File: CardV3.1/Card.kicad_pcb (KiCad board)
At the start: 2 copper layers, 85.6 x 54 mm, 6 parts, among them U1 M24LR04E-R

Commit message: Update Card.kicad_pcb
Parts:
- moved D1 2.01 mm to (119.0, 70.8)
- moved R1 1.25 mm to (114.0, 70.7)
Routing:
- net Net-(D1-Pad2): track 4.23 -> 3.44 mm
- net +3V3: track 7.20 -> 7.72 mm
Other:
- board text added: "Designed by Tingliang, Copyright © 2021 Tingliang Zhang CC BY-NC-ND"

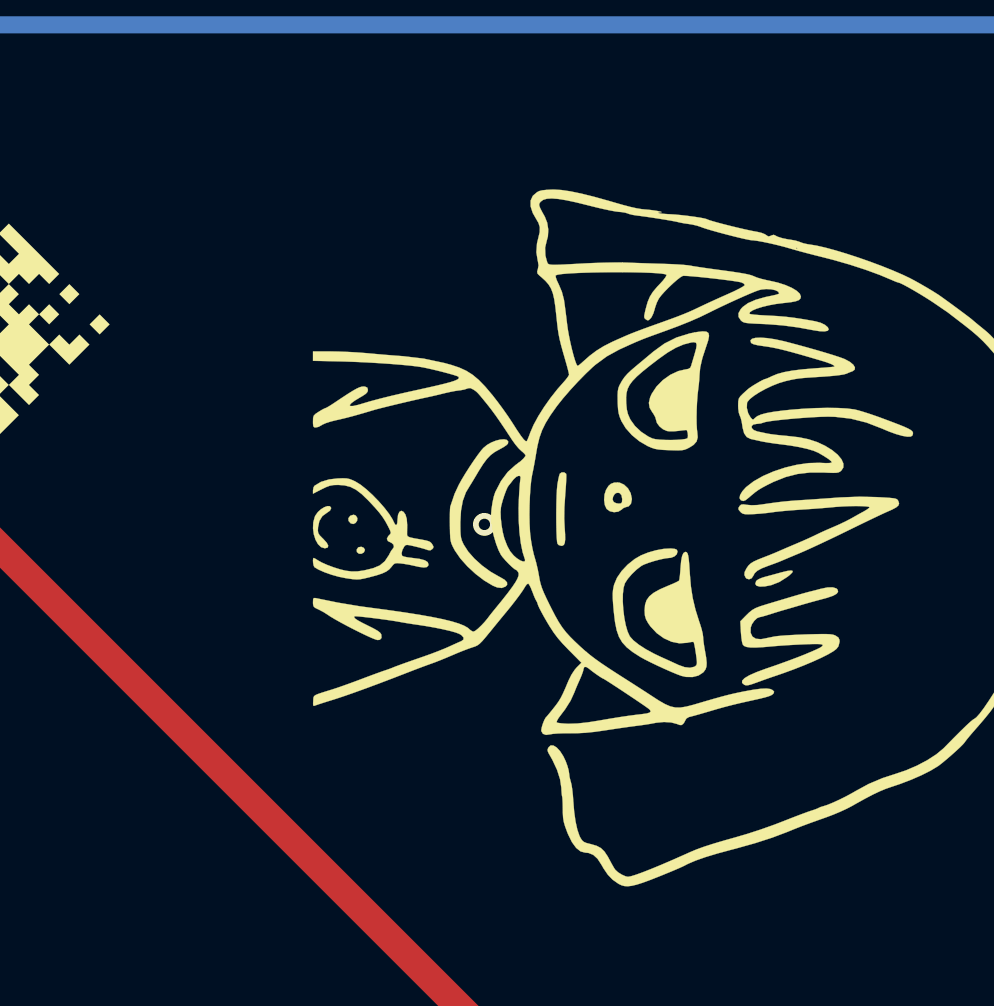
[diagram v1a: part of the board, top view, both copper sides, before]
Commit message: Add Interaction LOGO
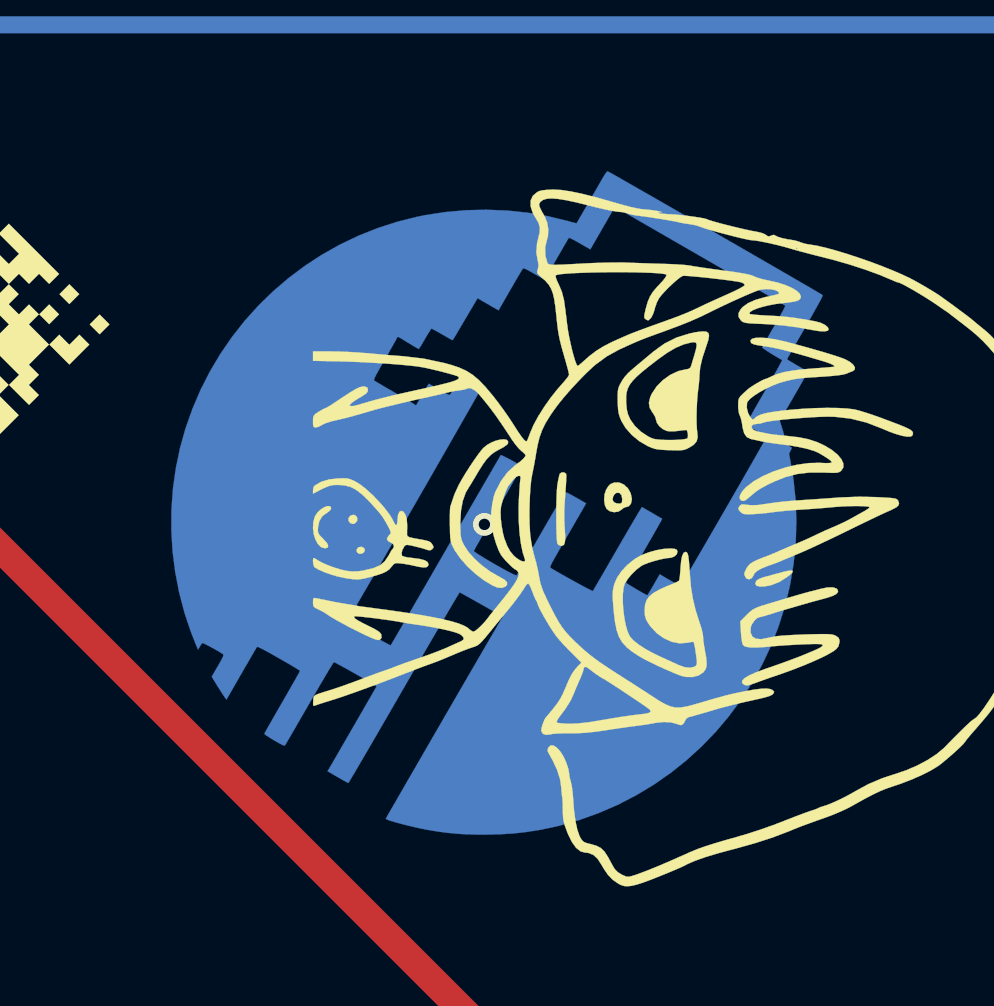
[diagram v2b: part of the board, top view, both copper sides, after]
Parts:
- added G***: LOGO, Card:FutureInteraction, B.Cu at (142.8, 73.0)

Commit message: Update Card.kicad_pcb
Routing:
- net (no net): vias 1 -> 0
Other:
- board text added: "T"
- board text removed: "Designed by Tingliang, Copyright © 2021 Tingliang Zhang CC BY-NC-ND"
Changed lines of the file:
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@@
-(kicad_pcb (version 20171130) (host pcbnew "(5.1.6)-1")
+(kicad_pcb (version 20171130) (host pcbnew "(5.1.9)-1")
   (general
     (thickness 1.6)
     (drawings 12)
-    (tracks 23)
+    (tracks 22)
     (zones 0)
     (modules 7)
@@
     (pad_drill 0.762)
     (pad_to_mask_clearance 0)
-    (aux_axis_origin 0 0)
+    (aux_axis_origin 142.8 73.01)
     (visible_elements 7FFFFFFF)
     (pcbplotparams
@@
     )
   )
-  (gr_text "Designed by Tingliang, Copyright © 2021 Tingliang Zhang CC BY-NC-ND" (at 154 99) (layer B.SilkS)
+  (gr_text T (at 104.14 99.06) (layer B.SilkS)
     (effects (font (size 1 1) (thickness 0.2) italic) (justify mirror))
   )
@@
   (gr_arc (start 103.18 96.82) (end 100 96.82) (angle -90) (layer Edge.Cuts) (width 0.05))
   (gr_arc (start 182.42 96.82) (end 182.42 100) (angle -90) (layer Edge.Cuts) (width 0.05))
-  (via (at 142.8 73.01) (size 0.8) (drill 0.4) (layers F.Cu B.Cu) (net 0))
   (segment (start 125 73) (end 151 99) (width 1) (layer F.Cu) (net 0))
   (via (at 110.991459 59.008541) (size 0.8) (drill 0.4) (layers F.Cu B.Cu) (net 1))

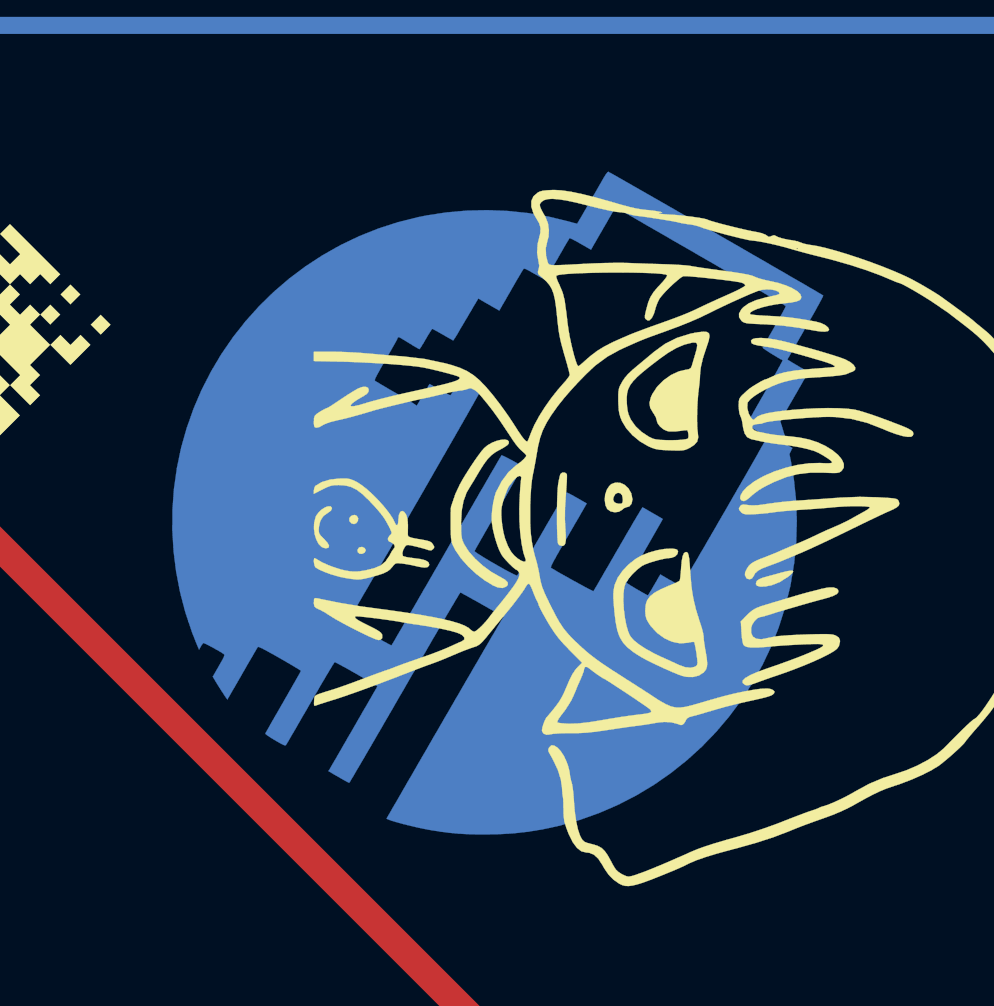
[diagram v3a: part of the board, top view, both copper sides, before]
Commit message: 断掉LOGO回路
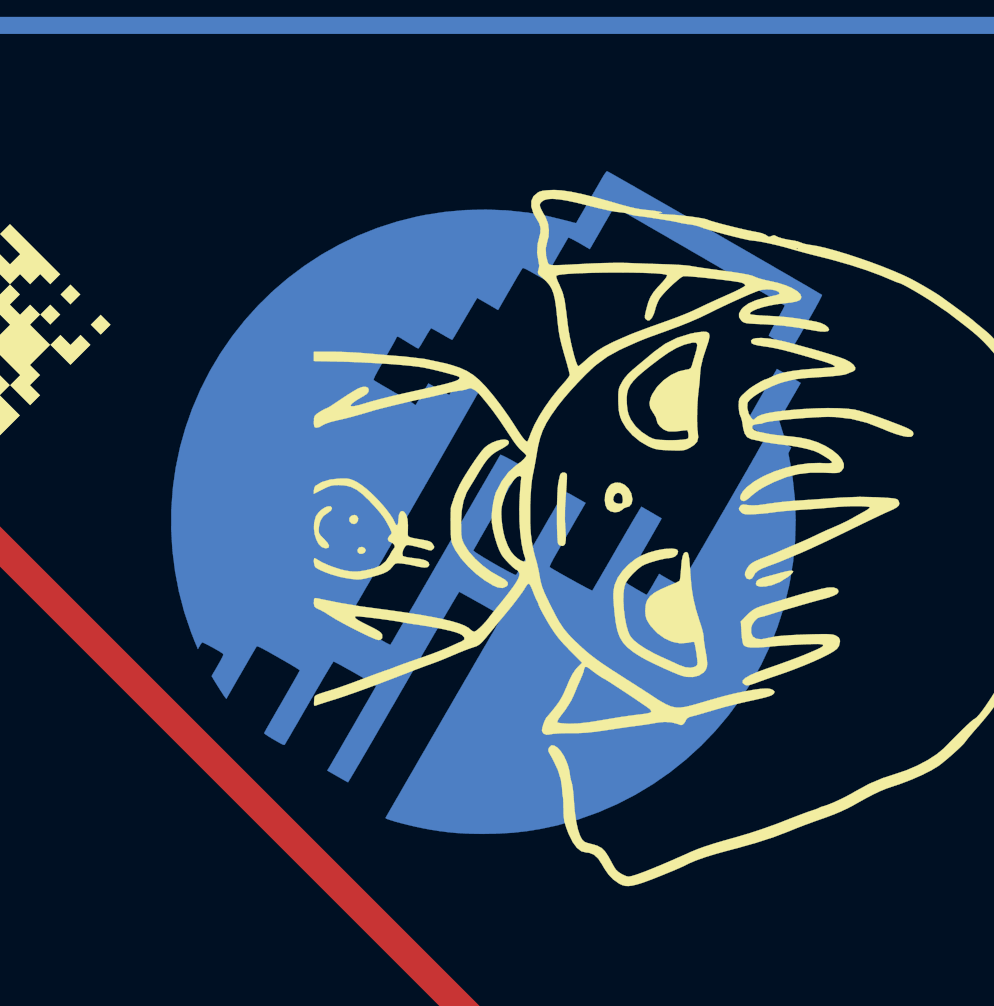
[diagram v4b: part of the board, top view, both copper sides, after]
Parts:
- removed the G*** at (142.8, 73.0)
- added G***: LOGO, Card:FutureInteractionDisconnect, B.Cu at (142.8, 73.0)
